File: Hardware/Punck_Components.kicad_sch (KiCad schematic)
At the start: 115 parts, among them J1 Conn_01x12_Female, J2 Conn_01x12_Female, J3 Conn_01x12_Female, J4 Conn_01x12_Female, J5 Debug_Header, J6 SWD_Header, J7 Eurorack_10_pin_power, Q1 MMBT3904, Q2 MMBT3904, Q3 MMBT3904, Q4 MMBT3904, Q5 MMBT3904, Q6 MMBT3904, Q7 MMBT3904, U1 TL074, U2 STM32H743ZITx, U3 W25Q128JVS, U4 PCM5100APW, U5 W25Q128JVS, U6 TPS561201, U7 LD1117-3.3-4Tab, Y1 8MHz 20pF

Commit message: Rough panel layout
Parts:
- added RESET1: SW_Push, Custom_Footprints:SW_SPST_EVQQ2, symbol Switch:SW_Push
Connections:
- net +3.3V is gone; now on net +3V3: C10.2, C11.2, C12.2, C13.2, C14.2, C2.2, C3.2, C31.1, C32.1, C4.2, C5.2, C6.2, C7.2, C8.2, C9.2, U2.108 (VDD), U2.121 (VDD), U2.131 (VDD), U2.144 (VDD), U2.17 (VDD), U2.30 (VDD), U2.39 (VDD), U2.52 (VDD), U2.6 (VBAT), U2.62 (VDD), U2.72 (VDD), U2.84 (VDD), U2.95 (VDD33_USB), U4.20 (DVDD)
- net GND: now also RESET1.2
- net RESET: no longer names the net of U2.25 (NRST)
- net RESET: now also RESET1.1
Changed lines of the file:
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@@
   (junction (at 77.47 224.79) (diameter 0) (color 0 0 0 0)
   )
+  (junction (at 21.59 57.15) (diameter 0) (color 0 0 0 0)
+  )
   (junction (at 111.76 25.4) (diameter 0) (color 0 0 0 0)
   )
@@
   (junction (at 223.52 167.64) (diameter 0) (color 0 0 0 0)
   )
-  (junction (at 236.22 167.64) (diameter 0) (color 0 0 0 0)
-  )
   (junction (at 21.59 64.77) (diameter 0) (color 0 0 0 0)
   )
@@
     (stroke (width 0) (type default) (color 0 0 0 0))
   )
+  (wire (pts (xy 29.21 49.53) (xy 21.59 49.53))
+    (stroke (width 0) (type solid) (color 0 0 0 0))
+  )
   (wire (pts (xy 295.91 80.01) (xy 295.91 73.66))
     (stroke (width 0) (type default) (color 0 0 0 0))
@@
     (stroke (width 0) (type default) (color 0 0 0 0))
   )
+  (wire (pts (xy 39.37 49.53) (xy 44.45 49.53))
+    (stroke (width 0) (type solid) (color 0 0 0 0))
+  )
   (wire (pts (xy 231.14 167.64) (xy 231.14 179.07))
     (stroke (width 0) (type default) (color 0 0 0 0))
@@
     (stroke (width 0) (type default) (color 0 0 0 0))
   )
-  (wire (pts (xy 41.91 49.53) (xy 44.45 49.53))
-    (stroke (width 0) (type default) (color 0 0 0 0))
-  )
   (wire (pts (xy 299.72 200.66) (xy 302.26 200.66))
     (stroke (width 0) (type default) (color 0 0 0 0))
@@
     (stroke (width 0) (type default) (color 0 0 0 0))
   )
+  (wire (pts (xy 21.59 49.53) (xy 21.59 57.15))
+    (stroke (width 0) (type solid) (color 0 0 0 0))
+  )
   (wire (pts (xy 314.96 213.36) (xy 314.96 214.63))
     (stroke (width 0) (type default) (color 0 0 0 0))
@@
     (effects (font (size 1.27 1.27)) (justify left bottom))
   )
-  (label "RESET" (at 41.91 49.53 180)
-    (effects (font (size 1.27 1.27)) (justify right bottom))
-  )
   (label "SAMPLER_B_SPEED_POT" (at 110.49 92.71 0)
     (effects (font (size 1.27 1.27)) (justify left bottom))
@@
     (pin "1")
   )
-  (symbol (lib_name "+3.3V_1") (lib_id "power:+3.3V") (at 236.22 167.64 0) (unit 1)
+  (symbol (lib_id "power:+3.3V") (at 236.22 167.64 0) (unit 1)
     (in_bom yes) (on_board yes)
     (property "Reference" "#PWR037" (id 0) (at 236.22 171.45 0)
@@
     (pin "2")
   )
+  (symbol (lib_id "Switch:SW_Push") (at 34.29 49.53 0) (mirror y) (unit 1)
+    (in_bom yes) (on_board yes)
+    (property "Reference" "RESET1" (id 0) (at 34.29 42.291 0))
+    (property "Value" "SW_Push" (id 1) (at 34.29 44.6024 0))
+    (property "Footprint" "Custom_Footprints:SW_SPST_EVQQ2" (id 2) (at 34.29 44.45 0)
+      (effects (font (size 1.27 1.27)) hide)
+    )
+    (property "Datasheet" "~" (id 3) (at 34.29 44.45 0)
+      (effects (font (size 1.27 1.27)) hide)
+    )
+    (pin "1")
+    (pin "2")
+  )
   (symbol (lib_id "Device:R_Small") (at 370.84 167.64 90) (unit 1)
     (in_bom yes) (on_board yes) (fields_autoplaced)
@@
     (pin "4")
   )
-  (symbol (lib_name "+3.3V_3") (lib_id "power:+3.3V") (at 58.42 25.4 0) (unit 1)
-    (in_bom yes) (on_board yes) (fields_autoplaced)
-    (property "Reference" "#PWR0101" (id 0) (at 58.42 29.21 0)
-      (effects (font (size 1.27 1.27)) hide)
-    )
-    (property "Value" "+3.3V" (id 1) (at 58.42 20.32 0))
-    (property "Footprint" "" (id 2) (at 58.42 25.4 0)
-      (effects (font (size 1.27 1.27)) hide)
-    )
-    (property "Datasheet" "" (id 3) (at 58.42 25.4 0)
-      (effects (font (size 1.27 1.27)) hide)
-    )
-    (pin "1")
-  )
   (symbol (lib_id "Transistor_BJT:2N3904") (at 378.46 68.58 0) (unit 1)
     (in_bom yes) (on_board yes) (fields_autoplaced)
@@
     (pin "4")
   )
+  (symbol (lib_id "power:+3.3V") (at 58.42 25.4 0) (unit 1)
+    (in_bom yes) (on_board yes)
+    (property "Reference" "#PWR0101" (id 0) (at 58.42 29.21 0)
+      (effects (font (size 1.27 1.27)) hide)
+    )
+    (property "Value" "+3.3V" (id 1) (at 59.69 22.86 0)
+      (effects (font (size 1.27 1.27)) (justify left))
+    )
+    (property "Footprint" "" (id 2) (at 58.42 25.4 0)
+      (effects (font (size 1.27 1.27)) hide)
+    )
+    (property "Datasheet" "" (id 3) (at 58.42 25.4 0)
+      (effects (font (size 1.27 1.27)) hide)
+    )
+    (pin "1")
+  )
   (symbol (lib_id "Device:R_Small") (at 381 157.48 180) (unit 1)
     (in_bom yes) (on_board yes) (fields_autoplaced)
@@
       (reference "#PWR082") (unit 1) (value "GND") (footprint "")
     )
-    (path "/3485846e-f3ed-417b-8bc9-6d15bdda8478"
+    (path "/4c297fc6-42da-4bb6-bab3-ad302add6e5c"
       (reference "#PWR0101") (unit 1) (value "+3.3V") (footprint "")
     )
@@
       (reference "R34") (unit 1) (value "10k") (footprint "Resistor_SMD:R_0603_1608Metric_Pad0.98x0.95mm_HandSolder")
     )
+    (path "/20ae5361-9b6d-4e9a-9353-876d2c321913"
+      (reference "RESET1") (unit 1) (value "SW_Push") (footprint "Custom_Footprints:SW_SPST_EVQQ2")
+    )
     (path "/00000000-0000-0000-0000-00006d82907d"

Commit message: Updated PCBs to match changes in panel; ground returns improved
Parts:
- removed R24: 1k, Resistor_SMD:R_0603_1608Metric_Pad0.98x0.95mm_HandSolder, symbol Device:R_Small
- renumbered R25 to R24, R26 to R25, R27 to R26, R28 to R27, R29 to R28, R30 to R29, R31 to R30, R32 to R31, R33 to R32, R34 to R33
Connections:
- net OH_LED is gone; now on net GND: J4.8 (Pin_8)
- net OH_LED_OUT is gone; now on net SEQ_SELECT: U2.96 (PC6)
- net CH_IN: now also J2.7 (Pin_7); no longer J2.6 (Pin_6)
- net GND: now also J2.1 (Pin_1); no longer J4.1 (Pin_1)
- net HIHAT_VOL_POT: now also J2.2 (Pin_2); no longer J2.1 (Pin_1)
- net KI_LED: now also J4.4 (Pin_4); no longer J4.5 (Pin_5)
- net MIDI_LEARN: now also J3.8 (Pin_8), U2.142 (PE1); no longer J2.10 (Pin_10), U2.69 (PB10)
- net OH_IN: now also J2.8 (Pin_8); no longer J2.7 (Pin_7)
- net SAMPLER_A_IN: now also J2.9 (Pin_9); no longer J2.8 (Pin_8)
- net SAMPLER_A_VOL_POT: now also J2.3 (Pin_3); no longer J2.2 (Pin_2)
- net SAMPLER_B_IN: now also J2.10 (Pin_10); no longer J2.9 (Pin_9)
- net SAMPLER_B_VOL_POT: now also J2.4 (Pin_4); no longer J2.3 (Pin_3)
- net SEQ_SELECT: now also J4.7 (Pin_7); no longer J2.11 (Pin_11), U2.78 (PD9)
- net SN_LED: now also J4.5 (Pin_5); no longer J4.6 (Pin_6)
- net TEMPO_POT: now also J2.6 (Pin_6); no longer J2.5 (Pin_5)
- net USB_DM: now also J4.2 (Pin_2); no longer J4.3 (Pin_3)
- net USB_DP: now also J4.1 (Pin_1); no longer J4.2 (Pin_2)
- net USB_VBUS: now also J4.3 (Pin_3); no longer J4.4 (Pin_4)
- net CH_BTN renamed HH_BTN
- net HH_BTN: now also J2.5 (Pin_5); no longer J2.4 (Pin_4)
- net CH_LED renamed HH_LED
- net HH_LED: now also J4.6 (Pin_6); no longer J4.7 (Pin_7)
- net CH_LED_OUT renamed HH_LED_OUT
- net OH_BTN: no longer names the net of U2.125 (PG10)
- net OH_BTN: no longer J3.8 (Pin_8)
- no-connect marks 51 -> 53
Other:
- moved on the sheet: R19, R21, R22, R24, R25

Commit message: More PCB tweaking
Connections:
- net AUDIO_OUT_L: now also J4.10 (Pin_10); no longer J4.9 (Pin_9)
- net GND: now also J4.9 (Pin_9)
- net TEMPO_OUT: now also J2.11 (Pin_11); no longer J4.10 (Pin_10)
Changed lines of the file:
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@@
   (junction (at 254 43.18) (diameter 0) (color 0 0 0 0)
   )
+  (junction (at 168.91 156.21) (diameter 0) (color 0 0 0 0)
+  )
   (junction (at 161.29 252.73) (diameter 0) (color 0 0 0 0)
   )
@@
     (stroke (width 0) (type default) (color 0 0 0 0))
   )
+  (wire (pts (xy 168.91 154.94) (xy 166.37 154.94))
+    (stroke (width 0) (type default) (color 0 0 0 0))
+  )
   (wire (pts (xy 81.28 25.4) (xy 81.28 27.94))
     (stroke (width 0) (type default) (color 0 0 0 0))
   )
+  (wire (pts (xy 168.91 157.48) (xy 168.91 156.21))
+    (stroke (width 0) (type default) (color 0 0 0 0))
+  )
   (wire (pts (xy 246.38 204.47) (xy 248.92 204.47))
     (stroke (width 0) (type default) (color 0 0 0 0))
@@
     (stroke (width 0) (type default) (color 0 0 0 0))
   )
+  (wire (pts (xy 166.37 157.48) (xy 168.91 157.48))
+    (stroke (width 0) (type default) (color 0 0 0 0))
+  )
   (wire (pts (xy 246.38 207.01) (xy 250.19 207.01))
     (stroke (width 0) (type default) (color 0 0 0 0))
@@
     (stroke (width 0) (type default) (color 0 0 0 0))
   )
+  (wire (pts (xy 168.91 156.21) (xy 168.91 154.94))
+    (stroke (width 0) (type default) (color 0 0 0 0))
+  )
   (wire (pts (xy 242.57 175.26) (xy 247.65 175.26))
     (stroke (width 0) (type default) (color 0 0 0 0))
@@
     (effects (font (size 1.27 1.27)) (justify left bottom))
   )
-  (label "AUDIO_OUT_L" (at 166.37 157.48 0)
+  (label "AUDIO_OUT_L" (at 166.37 160.02 0)
     (effects (font (size 1.27 1.27)) (justify left bottom))
   )
@@
     (effects (font (size 1.27 1.27)) (justify left bottom))
   )
-  (label "TEMPO_OUT" (at 166.37 160.02 0)
+  (label "TEMPO_OUT" (at 166.37 87.63 0)
     (effects (font (size 1.27 1.27)) (justify left bottom))
   )
@@
     (pin "2")
   )
-  (symbol (lib_id "power:GND") (at 166.37 154.94 90) (unit 1)
+  (symbol (lib_id "power:GND") (at 168.91 156.21 90) (unit 1)
     (in_bom yes) (on_board yes)
-    (property "Reference" "#PWR032" (id 0) (at 172.72 154.94 0)
+    (property "Reference" "#PWR032" (id 0) (at 175.26 156.21 0)
       (effects (font (size 1.27 1.27)) hide)
     )
-    (property "Value" "GND" (id 1) (at 171.45 153.67 90))
-    (property "Footprint" "" (id 2) (at 166.37 154.94 0)
+    (property "Value" "GND" (id 1) (at 173.99 154.94 90))
+    (property "Footprint" "" (id 2) (at 168.91 156.21 0)
       (effects (font (size 1.27 1.27)) hide)
     )
-    (property "Datasheet" "" (id 3) (at 166.37 154.94 0)
+    (property "Datasheet" "" (id 3) (at 168.91 156.21 0)
       (effects (font (size 1.27 1.27)) hide)
     )

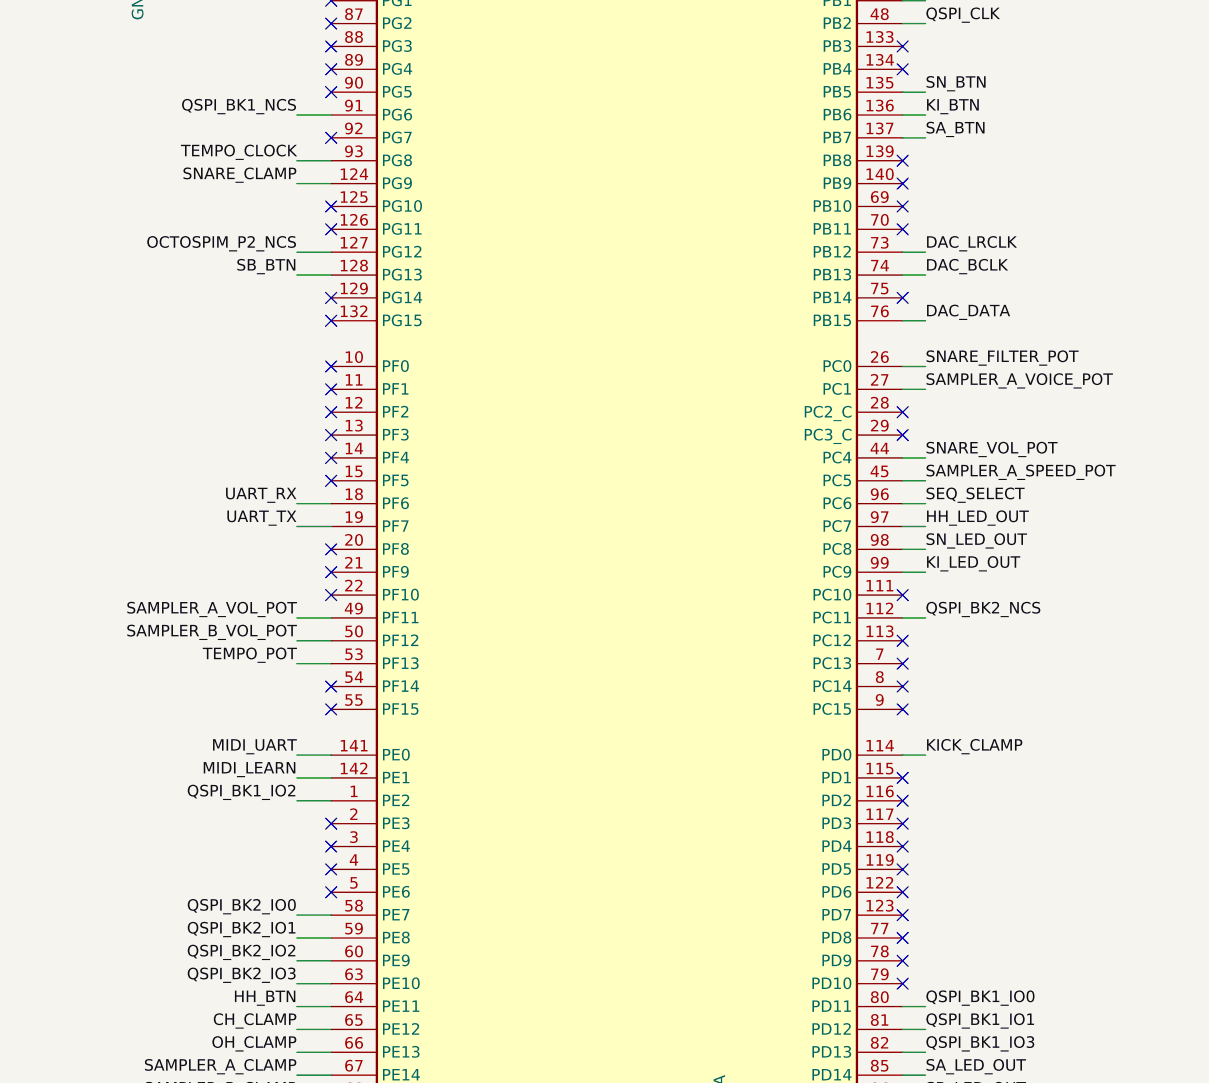
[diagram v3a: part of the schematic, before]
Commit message: Added Logo to panel
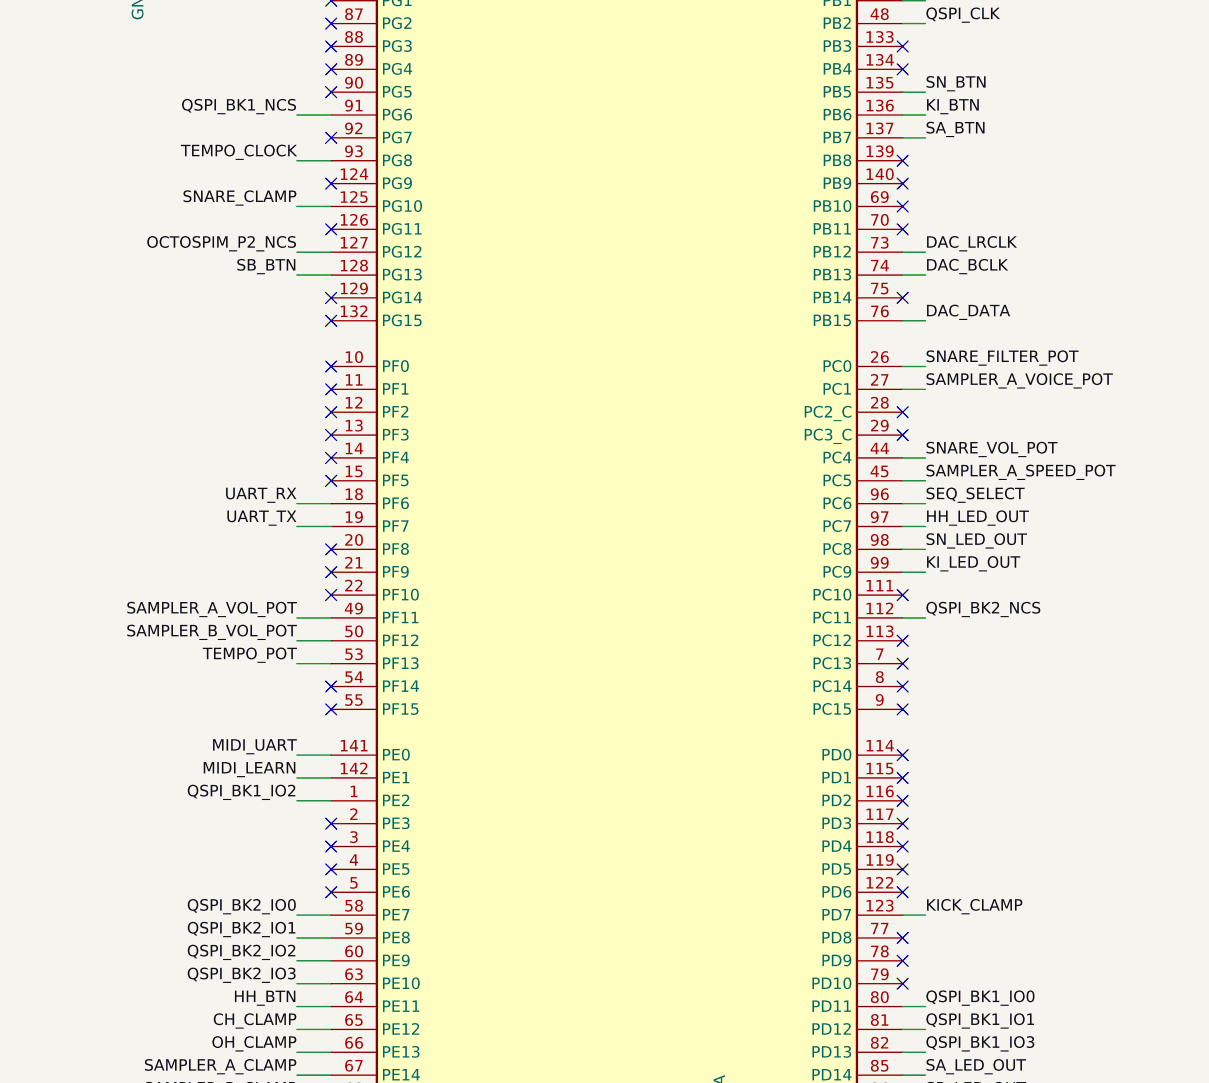
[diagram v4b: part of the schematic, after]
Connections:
- net KICK_CLAMP: now also U2.123 (PD7); no longer U2.114 (PD0)
- net SNARE_CLAMP: now also U2.125 (PG10); no longer U2.124 (PG9)
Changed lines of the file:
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@@
   (no_connect (at 107.95 191.77))
   (no_connect (at 44.45 194.31))
-  (no_connect (at 107.95 196.85))
+  (no_connect (at 107.95 179.07))
   (no_connect (at 44.45 138.43))
   (no_connect (at 44.45 100.33))
@@
   (no_connect (at 107.95 69.85))
   (no_connect (at 107.95 173.99))
-  (no_connect (at 44.45 118.11))
+  (no_connect (at 44.45 115.57))
   (no_connect (at 44.45 148.59))
   (no_connect (at 107.95 186.69))
@@
     (stroke (width 0) (type default) (color 0 0 0 0))
   )
-  (wire (pts (xy 40.64 115.57) (xy 44.45 115.57))
+  (wire (pts (xy 40.64 118.11) (xy 44.45 118.11))
     (stroke (width 0) (type default) (color 0 0 0 0))
   )
@@
     (stroke (width 0) (type default) (color 0 0 0 0))
   )
-  (wire (pts (xy 107.95 179.07) (xy 110.49 179.07))
+  (wire (pts (xy 107.95 196.85) (xy 110.49 196.85))
     (stroke (width 0) (type default) (color 0 0 0 0))
   )
@@
     (effects (font (size 1.27 1.27)) (justify left bottom))
   )
-  (label "KICK_CLAMP" (at 110.49 179.07 0)
+  (label "KICK_CLAMP" (at 110.49 196.85 0)
     (effects (font (size 1.27 1.27)) (justify left bottom))
   )
@@
     (effects (font (size 1.27 1.27)) (justify left bottom))
   )
-  (label "SNARE_CLAMP" (at 40.64 115.57 180)
+  (label "SNARE_CLAMP" (at 40.64 118.11 180)
     (effects (font (size 1.27 1.27)) (justify right bottom))
   )

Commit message: More PCB tweaks; rejigged bottom row of controls
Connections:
- net +3.3VA: now also R1.2, R11.2, R17.2
- net +3V3: no longer R1.2, R11.2, R17.2
- net AUDIO_OUT_L: now also J2.11 (Pin_11); no longer J4.10 (Pin_10)
- net AUDIO_OUT_R: now also J2.9 (Pin_9); no longer J4.11 (Pin_11)
- net CH_CLAMP: now also Q3.3 (C), R17.1, U2.125 (PG10); no longer Q4.3 (C), R20.1, U2.65 (PE12)
- net CH_IN: now also J3.10 (Pin_10), R18.1; no longer J2.7 (Pin_7), R23.1
- net GND: now also J4.10 (Pin_10), J4.11 (Pin_11); no longer J4.8 (Pin_8), J4.9 (Pin_9)
- net HH_LED: now also J4.8 (Pin_8); no longer J4.6 (Pin_6)
- net KICK_CLAMP: now also Q4.3 (C), R20.1, U2.115 (PD1); no longer Q2.3 (C), R11.1, U2.123 (PD7)
- net KICK_IN: now also J4.2 (Pin_2), R23.1; no longer J3.11 (Pin_11), R12.1
- net KI_LED: now also J4.6 (Pin_6); no longer J4.4 (Pin_4)
- net OH_CLAMP: now also Q2.3 (C), R11.1, U2.123 (PD7); no longer Q5.3 (C), R26.1, U2.66 (PE13)
- net OH_IN: now also J3.11 (Pin_11), R12.1; no longer J2.8 (Pin_8), R27.1
- net SAMPLER_A_IN: now also J2.7 (Pin_7); no longer J2.9 (Pin_9)
- net SAMPLER_B_IN: now also J2.8 (Pin_8); no longer J2.10 (Pin_10)
- net SEQ_SELECT: now also J4.9 (Pin_9); no longer J4.7 (Pin_7)
- net SNARE_CLAMP: now also Q5.3 (C), R26.1, U2.117 (PD3); no longer Q3.3 (C), R17.1, U2.125 (PG10)
- net SNARE_IN: now also J4.1 (Pin_1), R27.1; no longer J3.10 (Pin_10), R18.1
- net SN_LED: now also J4.7 (Pin_7); no longer J4.5 (Pin_5)
- net TEMPO_CLOCK: now also U2.78 (PD9); no longer U2.93 (PG8)
- net TEMPO_OUT: now also J2.10 (Pin_10); no longer J2.11 (Pin_11)
- net USB_DM: now also J4.4 (Pin_4); no longer J4.2 (Pin_2)
- net USB_DP: now also J4.3 (Pin_3); no longer J4.1 (Pin_1)
- net USB_VBUS: now also J4.5 (Pin_5); no longer J4.3 (Pin_3)

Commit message: Added test code to use PWM control on voice LEDs
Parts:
- R19, R21, R22, R24, R25: value 1k -> 560
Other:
- moved on the sheet: C1, C17, C20, C24, C25, R13, R14, R15, R16, R2, R3, R4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
